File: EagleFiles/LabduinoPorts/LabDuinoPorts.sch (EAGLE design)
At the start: 22 parts

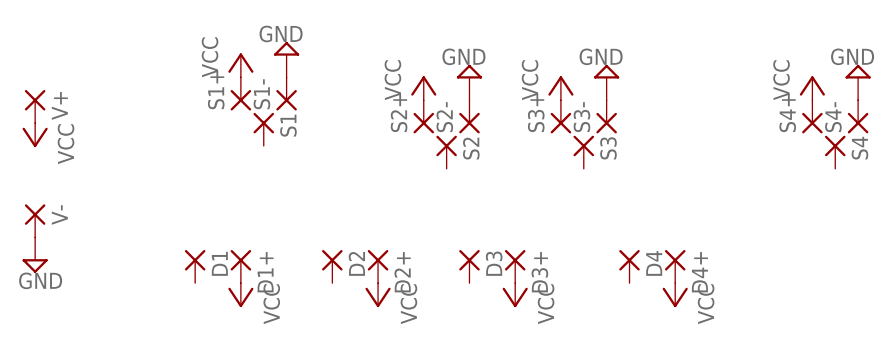
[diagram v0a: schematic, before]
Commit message: Eagle LabDuinoPorts Update
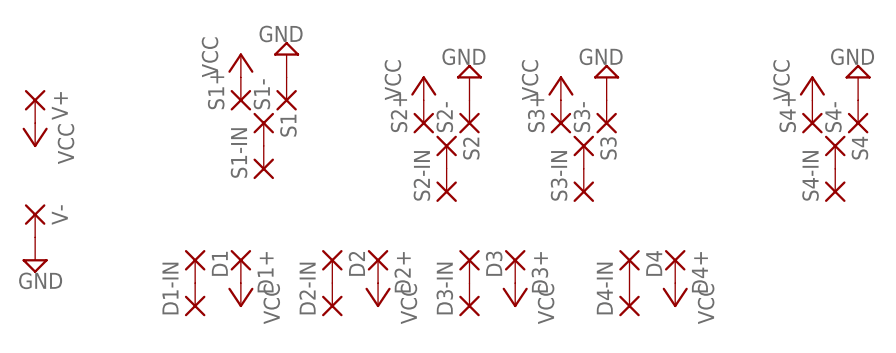
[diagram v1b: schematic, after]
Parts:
- added D1-IN, D2-IN, D3-IN, D4-IN, S1-IN, S2-IN, S3-IN, S4-IN: (no value), wirepad:2,54/0,9
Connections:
- new net N$1: S1-IN.P, S1.P
- new net N$2: S2-IN.P, S2.P
- new net N$3: S3-IN.P, S3.P
- new net N$4: S4-IN.P, S4.P
- new net N$5: D1-IN.P, D1.P
- new net N$6: D2-IN.P, D2.P
- new net N$7: D3-IN.P, D3.P
- new net N$8: D4-IN.P, D4.P
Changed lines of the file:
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@@
 <part name="V-" library="wirepad" deviceset="2,54/0,9" device=""/>
 <part name="SUPPLY5" library="supply2" deviceset="GND" device=""/>
+<part name="S1-IN" library="wirepad" deviceset="2,54/0,9" device=""/>
+<part name="S2-IN" library="wirepad" deviceset="2,54/0,9" device=""/>
+<part name="S3-IN" library="wirepad" deviceset="2,54/0,9" device=""/>
+<part name="S4-IN" library="wirepad" deviceset="2,54/0,9" device=""/>
+<part name="D1-IN" library="wirepad" deviceset="2,54/0,9" device=""/>
+<part name="D2-IN" library="wirepad" deviceset="2,54/0,9" device=""/>
+<part name="D3-IN" library="wirepad" deviceset="2,54/0,9" device=""/>
+<part name="D4-IN" library="wirepad" deviceset="2,54/0,9" device=""/>
 </parts>
 <sheets>
@@
 <instance part="V-" gate="1" x="-5.08" y="30.48" rot="R270"/>
 <instance part="SUPPLY5" gate="GND" x="-5.08" y="25.4"/>
+<instance part="S1-IN" gate="1" x="20.32" y="35.56" rot="R90"/>
+<instance part="S2-IN" gate="1" x="40.64" y="33.02" rot="R90"/>
+<instance part="S3-IN" gate="1" x="55.88" y="33.02" rot="R90"/>
+<instance part="S4-IN" gate="1" x="83.82" y="33.02" rot="R90"/>
+<instance part="D1-IN" gate="1" x="12.7" y="20.32" rot="R90"/>
+<instance part="D2-IN" gate="1" x="27.94" y="20.32" rot="R90"/>
+<instance part="D3-IN" gate="1" x="43.18" y="20.32" rot="R90"/>
+<instance part="D4-IN" gate="1" x="60.96" y="20.32" rot="R90"/>
 </instances>
 <busses>
@@
 </segment>
 </net>
+<net name="N$1" class="0">
+<segment>
+<pinref part="S1" gate="1" pin="P"/>
+<pinref part="S1-IN" gate="1" pin="P"/>
+</segment>
+</net>
+<net name="N$2" class="0">
+<segment>
+<pinref part="S2" gate="1" pin="P"/>
+<pinref part="S2-IN" gate="1" pin="P"/>
+</segment>
+</net>
+<net name="N$3" class="0">
+<segment>
+<pinref part="S3" gate="1" pin="P"/>
+<pinref part="S3-IN" gate="1" pin="P"/>
+</segment>
+</net>
+<net name="N$4" class="0">
+<segment>
+<pinref part="S4" gate="1" pin="P"/>
+<pinref part="S4-IN" gate="1" pin="P"/>
+</segment>
+</net>
+<net name="N$5" class="0">
+<segment>
+<pinref part="D1" gate="1" pin="P"/>
+<pinref part="D1-IN" gate="1" pin="P"/>
+</segment>
+</net>
+<net name="N$6" class="0">
+<segment>
+<pinref part="D2" gate="1" pin="P"/>
+<pinref part="D2-IN" gate="1" pin="P"/>
+</segment>
+</net>
+<net name="N$7" class="0">
+<segment>
+<pinref part="D3" gate="1" pin="P"/>
+<pinref part="D3-IN" gate="1" pin="P"/>
+</segment>
+</net>
+<net name="N$8" class="0">
+<segment>
+<pinref part="D4" gate="1" pin="P"/>
+<pinref part="D4-IN" gate="1" pin="P"/>
+</segment>
+</net>
